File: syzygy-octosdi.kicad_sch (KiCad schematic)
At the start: 7 parts, among them CN1 QTH-020-01-F-D-DP-A, X1 SX7DF148_500B20F30DNN

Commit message: implement schematic review feedback
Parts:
- added R68, R69: 10k, Resistor_SMD:R_0603_1608Metric, symbol Device:R
- C1: renamed from C13; value 10n -> 100n
- renumbered R42 to R1, R44 to R2
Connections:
- net I2C.SCL: now also R69.2
- net I2C.SDA: now also R68.2
- net VIO: now also R68.1, R69.1
- net VIO_GOOD: now reaches X1.1 (tri-state)
- no-connect marks 12 -> 11
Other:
- sheet Quad ports: added VIO_GOOD, ~{VIO_GOOD}; removed none
- sheet Quad1 ports: added VIO_GOOD, ~{VIO_GOOD}; removed none
- sheet SmartVIO ports: added VIO, VIO_GOOD, ~{VIO_GOOD}; removed none
- moved on the sheet: R1, R2

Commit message: substitute bnc connector for better max freq
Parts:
- renumbered R69 to R2, R2 to R3, R68 to R4
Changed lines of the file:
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@@
 		(in_pos_files yes)
 		(dnp no)
-		(property "Reference" "R69"
+		(property "Reference" "R2"
 			(at 251.46 83.8199 0)
 			(show_name no)
@@
 			(project "syzygy-octosdi"
 				(path "/cb0cdcc9-6b9b-4b74-8146-9043de7999b1"
-					(reference "R69")
+					(reference "R2")
 					(unit 1)
 				)
@@
 		(in_pos_files yes)
 		(dnp no)
-		(property "Reference" "R68"
+		(property "Reference" "R4"
 			(at 260.35 83.8199 0)
 			(show_name no)
@@
 			(project "syzygy-octosdi"
 				(path "/cb0cdcc9-6b9b-4b74-8146-9043de7999b1"
-					(reference "R68")
+					(reference "R4")
 					(unit 1)
 				)
@@
 		(in_pos_files yes)
 		(dnp no)
-		(property "Reference" "#PWR08"
+		(property "Reference" "#PWR09"
 			(at 172.72 71.12 0)
 			(hide yes)
@@
 			(project "syzygy-octosdi"
 				(path "/cb0cdcc9-6b9b-4b74-8146-9043de7999b1"
-					(reference "#PWR08")
+					(reference "#PWR09")
 					(unit 1)
 				)
@@
 		(in_pos_files yes)
 		(dnp no)
-		(property "Reference" "R2"
+		(property "Reference" "R3"
 			(at 257.81 52.0699 0)
 			(show_name no)
@@
 			(project "syzygy-octosdi"
 				(path "/cb0cdcc9-6b9b-4b74-8146-9043de7999b1"
-					(reference "R2")
+					(reference "R3")
 					(unit 1)
 				)
@@
 		(dnp no)
 		(fields_autoplaced yes)
-		(property "Reference" "#PWR09"
+		(property "Reference" "#PWR010"
 			(at 222.25 144.78 0)
 			(hide yes)
@@
 			(project "syzygy-octosdi"
 				(path "/cb0cdcc9-6b9b-4b74-8146-9043de7999b1"
-					(reference "#PWR09")
+					(reference "#PWR010")
 					(unit 1)
 				)
@@
 		(dnp no)
 		(fields_autoplaced yes)
-		(property "Reference" "#PWR0120"
+		(property "Reference" "#PWR08"
 			(at 161.29 87.63 0)
 			(hide yes)
@@
 			(project "syzygy-octosdi"
 				(path "/cb0cdcc9-6b9b-4b74-8146-9043de7999b1"
-					(reference "#PWR0120")
-					(unit 1)
-				)
+					(reference "#PWR08")
+					(unit 1)
+				)

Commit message: split gpio expanders by inputs/outputs instead of quads
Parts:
- C1, R1, R2, R3, R4: KiLib_Generator (none) -> SMD_2terminal_chip_molded
- H1, H2: KiLib_Generator (none) -> mounting_hardware/mounting_hole
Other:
- sheet Quad renamed Inputs
- sheet Quad1 renamed Outputs
- sheet Inputs: file quad.kicad_sch -> inputs.kicad_sch
- sheet Inputs ports: added RX2{P,N}, RX3{P,N}; removed TX0{P,N}, TX1{P,N}, VIO_GOOD
- sheet Outputs: file quad.kicad_sch -> outputs.kicad_sch
- sheet Outputs ports: added TX2{P,N}, TX3{P,N}; removed RX0{P,N}, RX1{P,N}, ~{VIO_GOOD}
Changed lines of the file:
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@@
 	(bus
 		(pts
-			(xy 165.1 53.34) (xy 175.26 53.34)
+			(xy 165.1 52.07) (xy 175.26 52.07)
 		)
 		(stroke
@@
 	(wire
 		(pts
-			(xy 165.1 49.53) (xy 175.26 49.53)
-		)
-		(stroke
-			(width 0)
-			(type default)
-		)
-	)
-	(wire
-		(pts
 			(xy 240.03 91.44) (xy 254 91.44)
 		)
@@
 	(bus
 		(pts
-			(xy 165.1 82.55) (xy 175.26 82.55)
+			(xy 165.1 81.28) (xy 175.26 81.28)
 		)
 		(stroke
@@
 	(wire
 		(pts
-			(xy 165.1 76.2) (xy 175.26 76.2)
-		)
-		(stroke
-			(width 0)
-			(type default)
-		)
-	)
-	(wire
-		(pts
 			(xy 165.1 87.63) (xy 175.26 87.63)
 		)
@@
 	(wire
 		(pts
-			(xy 165.1 78.74) (xy 175.26 78.74)
+			(xy 165.1 76.2) (xy 175.26 76.2)
 		)
 		(stroke
@@
 		)
 	)
-	(label "TX1{P,N}"
+	(label "RX3{P,N}"
 		(at 210.82 55.88 180)
 		(effects
@@
 	)
 	(label "VIO_GOOD"
-		(at 165.1 78.74 0)
+		(at 165.1 76.2 0)
 		(effects
 			(font
@@
 		)
 	)
-	(label "RX2{P,N}"
+	(label "TX0{P,N}"
 		(at 210.82 77.47 180)
 		(effects
@@
 		)
 	)
-	(label "TX2{P,N}"
+	(label "TX1{P,N}"
 		(at 210.82 80.01 180)
 		(effects
@@
 		)
 	)
-	(label "RX3{P,N}"
+	(label "TX2{P,N}"
 		(at 210.82 82.55 180)
 		(effects
@@
 		)
 	)
-	(label "~{VIO_GOOD}"
-		(at 165.1 76.2 0)
-		(effects
-			(font
-				(size 1.27 1.27)
-			)
-			(justify left bottom)
-		)
-	)
 	(label "~{INT}"
 		(at 165.1 87.63 0)
@@
 		)
 	)
-	(label "RX1{P,N}"
+	(label "RX2{P,N}"
 		(at 210.82 53.34 180)
 		(effects
@@
 	)
 	(label "I2C{I2C}"
-		(at 165.1 53.34 0)
+		(at 165.1 52.07 0)
 		(effects
 			(font
@@
 		)
 	)
-	(label "VIO_GOOD"
-		(at 165.1 49.53 0)
-		(effects
-			(font
-				(size 1.27 1.27)
-			)
-			(justify left bottom)
-		)
-	)
-	(label "TX0{P,N}"
+	(label "RX1{P,N}"
 		(at 210.82 50.8 180)
 		(effects
@@
 	)
 	(label "I2C{I2C}"
-		(at 165.1 82.55 0)
+		(at 165.1 81.28 0)
 		(effects
 			(font
@@
 			)
 		)
+		(property "KiLib_Generator" "SMD_2terminal_chip_molded"
+			(at 254 85.09 0)
+			(hide yes)
+			(show_name no)
+			(do_not_autoplace no)
+			(effects
+				(font
+					(size 1.27 1.27)
+				)
+			)
+		)
 		(pin "1"
 		)
@@
 			)
 		)
+		(property "KiLib_Generator" "SMD_2terminal_chip_molded"
+			(at 262.89 85.09 0)
+			(hide yes)
+			(show_name no)
+			(do_not_autoplace no)
+			(effects
+				(font
+					(size 1.27 1.27)
+				)
+			)
+		)
 		(pin "1"
 		)
@@
 			)
 		)
+		(property "KiLib_Generator" "mounting_hardware/mounting_hole"
+			(at 209.55 133.35 0)
+			(hide yes)
+			(show_name no)
+			(do_not_autoplace no)
+			(effects
+				(font
+					(size 1.27 1.27)
+				)
+			)
+		)
 		(pin "1"
 		)
@@
 			)
 		)
+		(property "KiLib_Generator" "SMD_2terminal_chip_molded"
+			(at 260.35 53.34 0)
+			(hide yes)
+			(show_name no)
+			(do_not_autoplace no)
+			(effects
+				(font
+					(size 1.27 1.27)
+				)
+			)
+		)
 		(pin "1"
 		)
@@
 			)
 		)
+		(property "KiLib_Generator" "SMD_2terminal_chip_molded"
+			(at 251.46 53.34 0)
+			(hide yes)
+			(show_name no)
+			(do_not_autoplace no)
+			(effects
+				(font
+					(size 1.27 1.27)
+				)
+			)
+		)
 		(pin "1"
 		)
@@
 			)
 		)
+		(property "KiLib_Generator" "SMD_2terminal_chip_molded"
+			(at 133.35 132.08 0)
+			(hide yes)
+			(show_name no)
+			(do_not_autoplace no)
+			(effects
+				(font
+					(size 1.27 1.27)
+				)
+			)
+		)
 		(pin "1"
 		)
@@
 			)
 		)
+		(property "KiLib_Generator" "mounting_hardware/mounting_hole"
+			(at 232.41 133.35 0)
+			(hide yes)
+			(show_name no)
+			(do_not_autoplace no)
+			(effects
+				(font
+					(size 1.27 1.27)
+				)
+			)
+		)
 		(pin "1"
 		)
@@
 			(color 0 0 0 0)
 		)
-		(property "Sheetname" "Quad1"
+		(property "Sheetname" "Outputs"
 			(at 175.26 70.4084 0)
 			(show_name no)
@@
 			)
 		)
-		(property "Sheetfile" "quad.kicad_sch"
+		(property "Sheetfile" "outputs.kicad_sch"
 			(at 175.26 93.2946 0)
 			(show_name no)
@@
 		)
 		(pin "I2C{I2C}" bidirectional
-			(at 175.26 82.55 180)
+			(at 175.26 81.28 180)
 			(effects
 				(font
@@
 			)
 		)
-		(pin "RX0{P,N}" bidirectional
+		(pin "TX0{P,N}" bidirectional
 			(at 199.39 77.47 0)
 			(effects
@@
 			)
 		)
-		(pin "TX0{P,N}" bidirectional
+		(pin "TX1{P,N}" bidirectional
 			(at 199.39 80.01 0)
 			(effects
@@
 			)
 		)
-		(pin "RX1{P,N}" bidirectional
+		(pin "TX2{P,N}" bidirectional
 			(at 199.39 82.55 0)
 			(effects
@@
 			)
 		)
-		(pin "TX1{P,N}" bidirectional
+		(pin "TX3{P,N}" bidirectional
 			(at 199.39 85.09 0)
 			(effects
@@
 			)
 		)
-		(pin "~{VIO_GOOD}" input
-			(at 175.26 76.2 180)
-			(effects
-				(font
-					(size 1.27 1.27)
-				)
-				(justify left)
-			)
-		)
 		(pin "VIO_GOOD" input
-			(at 175.26 78.74 180)
+			(at 175.26 76.2 180)
 			(effects
 				(font
@@
 			(color 0 0 0 0)
 		)
-		(property "Sheetname" "Quad"
+		(property "Sheetname" "Inputs"
 			(at 175.26 41.1984 0)
 			(show_name no)
@@
 			)
 		)
-		(property "Sheetfile" "quad.kicad_sch"
+		(property "Sheetfile" "inputs.kicad_sch"
 			(at 175.26 64.0846 0)
 			(show_name no)
@@
 		)
 		(pin "I2C{I2C}" bidirectional
-			(at 175.26 53.34 180)
+			(at 175.26 52.07 180)
 			(effects
 				(font
@@
 			)
 		)
-		(pin "TX0{P,N}" bidirectional
+		(pin "RX1{P,N}" bidirectional
 			(at 199.39 50.8 0)
 			(effects
@@
 			)
 		)
-		(pin "RX1{P,N}" bidirectional
+		(pin "RX2{P,N}" bidirectional
 			(at 199.39 53.34 0)
 			(effects
@@
 			)
 		)
-		(pin "TX1{P,N}" bidirectional
+		(pin "RX3{P,N}" bidirectional
 			(at 199.39 55.88 0)
 			(effects
@@
 			(effects
 				(font
-					(size 1.27 1.27)
-				)
-				(justify left)
-			)
-		)
-		(pin "VIO_GOOD" input
-			(at 175.26 49.53 180)
-			(effects
-				(font

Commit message: route the smartvio mcu and the gpio expanders
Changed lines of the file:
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@@
 	)
 	(bus_entry
-		(at 102.87 132.08)
+		(at 105.41 132.08)
 		(size -2.54 2.54)
 		(stroke
@@
 	)
 	(bus_entry
-		(at 102.87 129.54)
+		(at 105.41 129.54)
 		(size -2.54 2.54)
 		(stroke
@@
 	(bus
 		(pts
-			(xy 115.57 129.54) (xy 102.87 129.54)
+			(xy 118.11 129.54) (xy 105.41 129.54)
 		)
 		(stroke
@@
 	(bus
 		(pts
-			(xy 102.87 129.54) (xy 102.87 132.08)
+			(xy 105.41 129.54) (xy 105.41 132.08)
 		)
 		(stroke
@@
 	(wire
 		(pts
-			(xy 100.33 132.08) (xy 87.63 132.08)
+			(xy 102.87 132.08) (xy 87.63 132.08)
 		)
 		(stroke
@@
 	(wire
 		(pts
-			(xy 100.33 134.62) (xy 87.63 134.62)
+			(xy 102.87 134.62) (xy 87.63 134.62)
 		)
 		(stroke
@@
 	)
 	(label "REFCLK{P,N}"
-		(at 115.57 129.54 180)
+		(at 118.11 129.54 180)
 		(effects
 			(font
@@
 		)
 	)
+	(rule_area
+		(exclude_from_sim no)
+		(in_bom yes)
+		(on_board yes)
+		(dnp no)
+		(polyline
+			(pts
+				(xy 99.695 127) (xy 99.695 136.525) (xy 100.965 136.525) (xy 100.965 127)
+			)
+			(stroke
+				(width 0)
+				(type dash)
+			)
+			(fill
+				(type none)
+			)
+		)
+	)
+	(netclass_flag ""
+		(length 2.54)
+		(shape round)
+		(at 100.33 127 0)
+		(effects
+			(font
+				(size 1.27 1.27)
+			)
+			(justify left bottom)
+		)
+		(property "Netclass" "100 Ohm Diff"
+			(at 97.536 122.428 0)
+			(show_name no)
+			(do_not_autoplace no)
+			(effects
+				(font
+					(size 1.27 1.27)
+				)
+				(justify left)
+			)
+		)
+		(property "Component Class" ""
+			(at -85.09 62.23 0)
+			(show_name no)
+			(do_not_autoplace no)
+			(effects
+				(font
+					(size 1.27 1.27)
+					(italic yes)
+				)
+			)
+		)
+	)

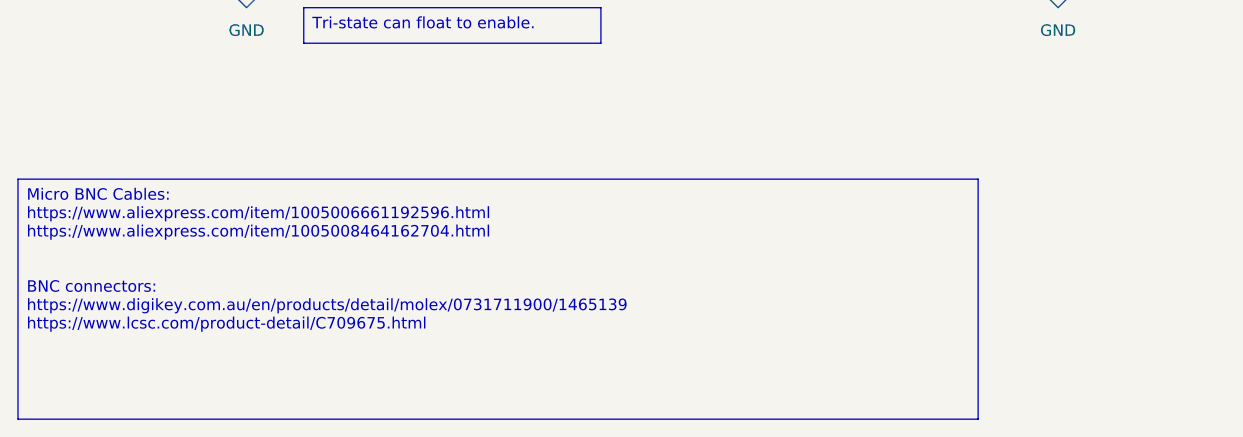
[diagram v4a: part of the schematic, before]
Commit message: route all the low speed io and start 3v3
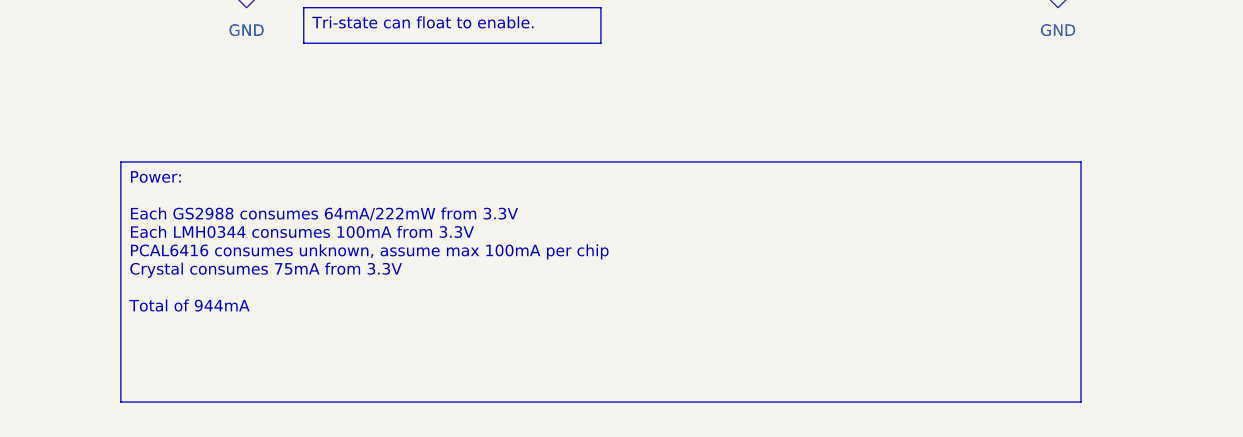
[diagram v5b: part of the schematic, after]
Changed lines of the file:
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@@
 	(generator_version "10.0")
 	(paper "A4")
-	(text_box "Micro BNC Cables:\nhttps://www.aliexpress.com/item/1005006661192596.html\nhttps://www.aliexpress.com/item/1005008464162704.html\n\n\nBNC connectors:\nhttps://www.digikey.com.au/en/products/detail/molex/0731711900/1465139\nhttps://www.lcsc.com/product-detail/C709675.html"
+	(text_box "Power:\n\nEach GS2988 consumes 64mA/222mW from 3.3V\nEach LMH0344 consumes 100mA from 3.3V\nPCAL6416 consumes unknown, assume max 100mA per chip\nCrystal consumes 75mA from 3.3V\n\nTotal of 944mA"
 		(exclude_from_sim no)
-		(at 17.78 157.48 0)
+		(at 29.21 155.575 0)
 		(size 106.68 26.67)
 		(margins 0.9525 0.9525 0.9525 0.9525)

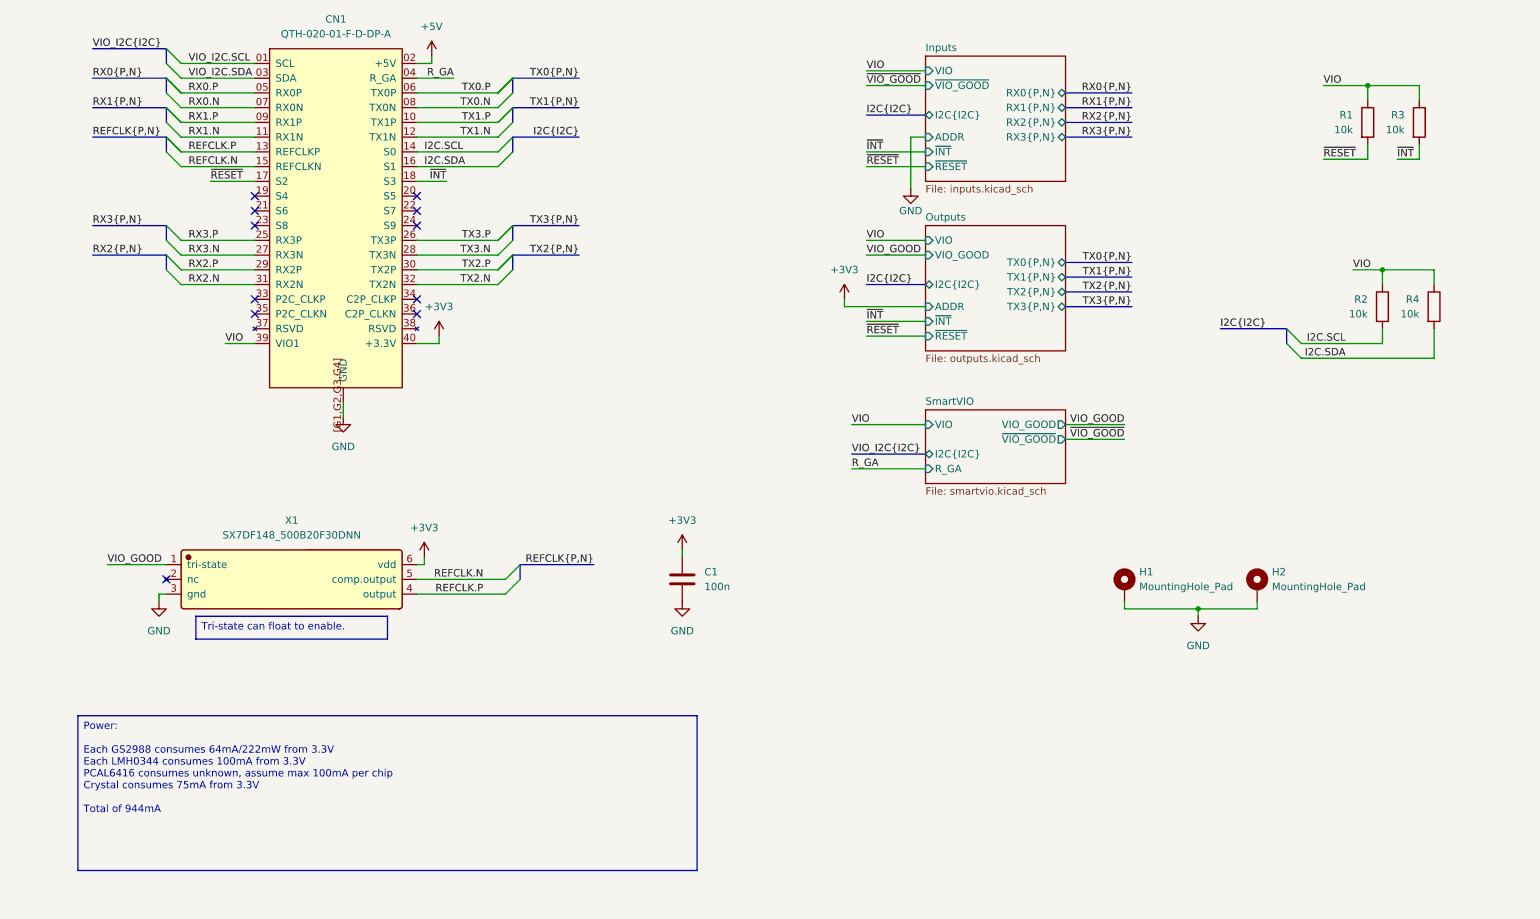
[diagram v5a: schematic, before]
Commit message: fixes following review and more mounting holes
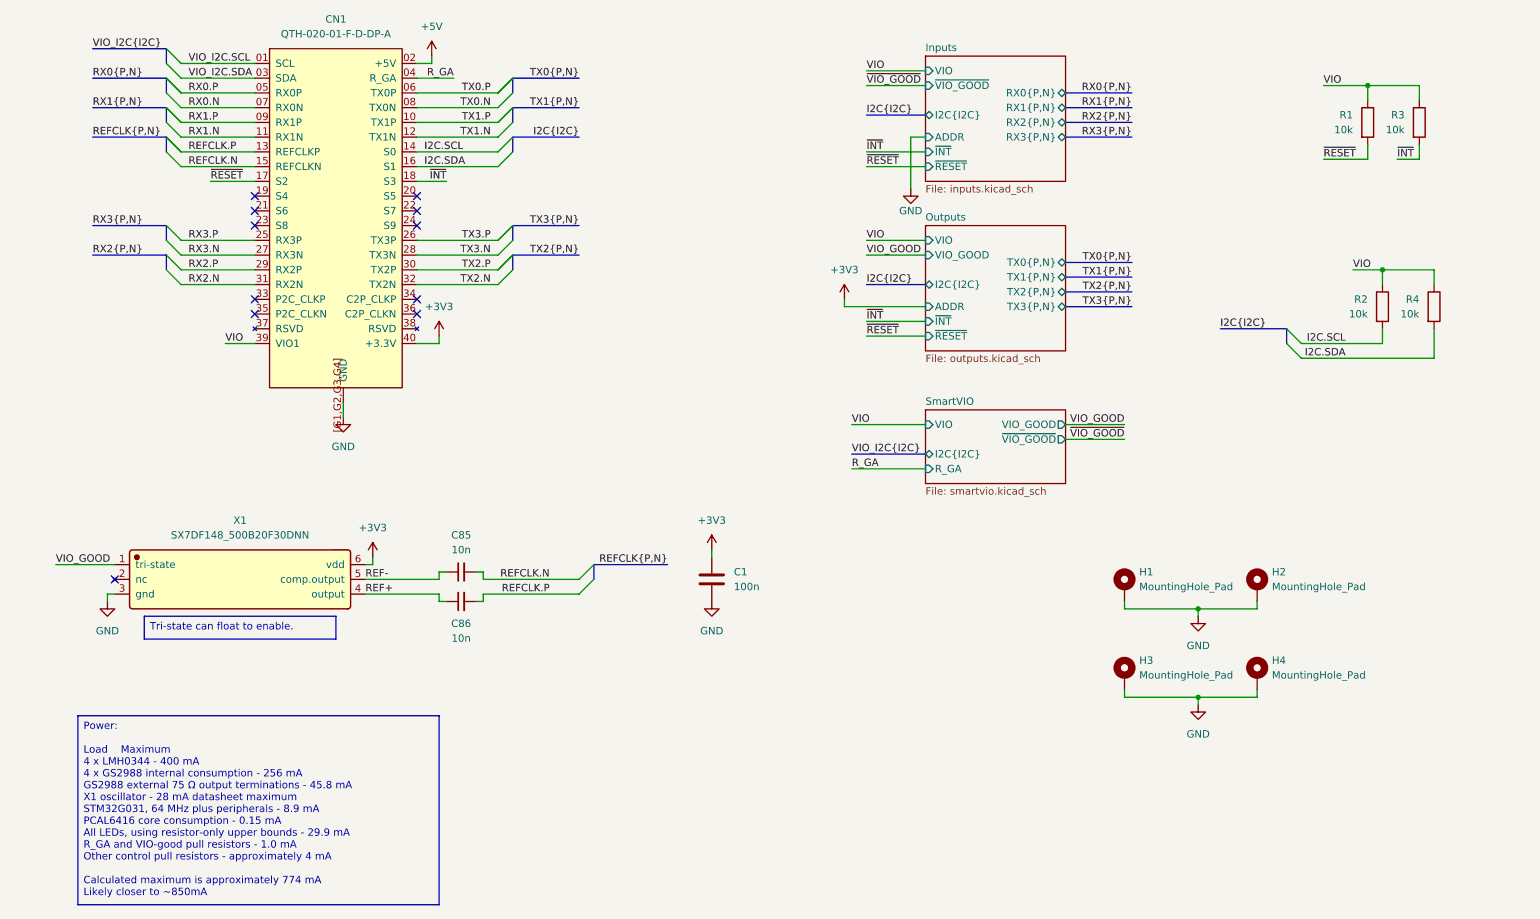
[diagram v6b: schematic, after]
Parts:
- added C85, C86: 10n, Capacitor_SMD:C_0402_1005Metric, symbol Device:C_Small
- added H3, H4: MountingHole_Pad, MountingHole:MountingHole_3.2mm_M3_Pad, symbol Mechanical:MountingHole_Pad
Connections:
- net GND: now also H3.1, H4.1
- net REFCLK.N: now also C85.2; no longer X1.5 (comp.output)
- net REFCLK.P: now also C86.2; no longer X1.4 (output)
- new net REF+: C86.1, X1.4 (output)
- new net REF-: C85.1, X1.5 (comp.output)
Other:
- moved on the sheet: C1, X1
